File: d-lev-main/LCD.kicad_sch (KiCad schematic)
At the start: 9 parts, among them Q1 MMBT3904

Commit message: clean up 3d models
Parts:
- DS2: footprint LCD_LCD-20X4B -> d-lev:ERM2004-1
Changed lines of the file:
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@@
       (effects (font (size 1.27 1.27)))
     )
-    (property "Footprint" "LCD_LCD-20X4B" (at 149.86 102.87 0)
+    (property "Footprint" "d-lev:ERM2004-1" (at 149.86 102.87 0)
       (effects (font (size 1.27 1.27)) (justify bottom) hide)
     )

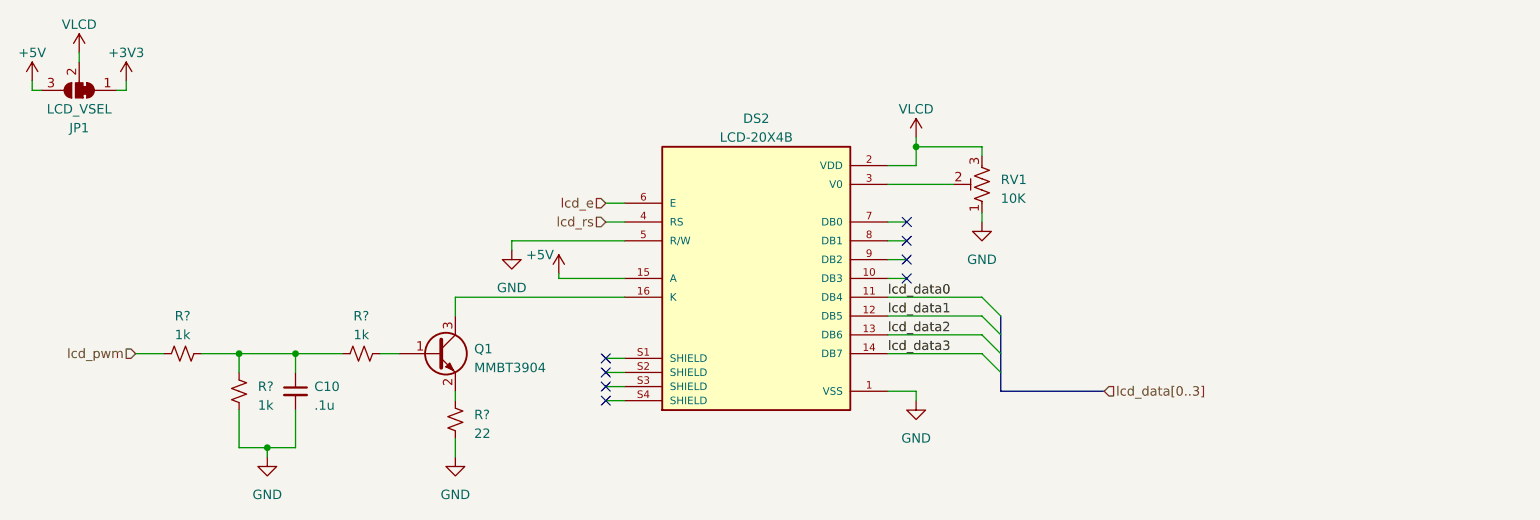
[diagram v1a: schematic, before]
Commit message: Level shifters and rearrange encoders
* WIP: use net buses more effectively to organize encoder signals
* Add application note for level shifters
* Add level shifters for UART, change MIDI level shifter BJT to FET
* Add MIDI_HI pull-up on d-lev-io board
* Add/change some footprints
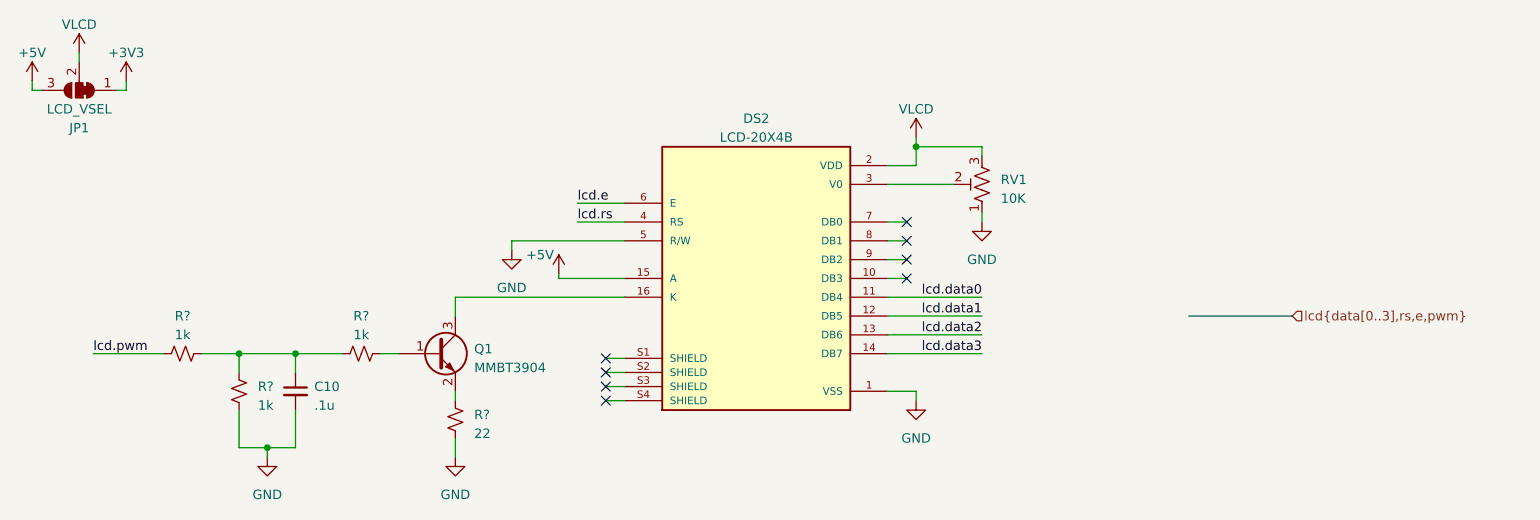
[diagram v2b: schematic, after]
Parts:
- C10: footprint (none) -> Capacitor_SMD:C_0805_2012Metric_Pad1.18x1.45mm_HandSolder
- JP1: footprint (none) -> Jumper:SolderJumper-3_P1.3mm_Bridged2Bar12_RoundedPad1.0x1.5mm_NumberLabels
- R? (x4): footprint (none) -> Resistor_SMD:R_0805_2012Metric_Pad1.20x1.40mm_HandSolder
- RV1: footprint (none) -> Potentiometer_SMD:Potentiometer_Bourns_3269P_Horizontal
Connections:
- net lcd_data0 renamed lcd.data0
- net lcd_data1 renamed lcd.data1
- net lcd_data2 renamed lcd.data2
- net lcd_data3 renamed lcd.data3
- net lcd_e renamed lcd.e
- net lcd_pwm renamed lcd.pwm
- net lcd_rs renamed lcd.rs
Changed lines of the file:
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@@
   (no_connect (at 129.54 115.57))
   (no_connect (at 170.18 102.87))
-  (bus_entry (at 180.34 105.41) (size 2.54 2.54)
-    (stroke (width 0) (type default))
-  )
-  (bus_entry (at 180.34 107.95) (size 2.54 2.54)
-    (stroke (width 0) (type default))
-  )
-  (bus_entry (at 180.34 110.49) (size 2.54 2.54)
-    (stroke (width 0) (type default))
-  )
-  (bus_entry (at 180.34 113.03) (size 2.54 2.54)
-    (stroke (width 0) (type default))
-  )
   (wire (pts (xy 80.01 125.73) (xy 83.82 125.73))
     (stroke (width 0) (type default))
@@
     (stroke (width 0) (type default))
   )
-  (wire (pts (xy 129.54 95.25) (xy 132.08 95.25))
+  (wire (pts (xy 125.73 95.25) (xy 132.08 95.25))
     (stroke (width 0) (type default))
   )
@@
     (stroke (width 0) (type default))
   )
-  (bus (pts (xy 182.88 107.95) (xy 182.88 110.49))
-    (stroke (width 0) (type default))
-  )
   (wire (pts (xy 132.08 115.57) (xy 129.54 115.57))
     (stroke (width 0) (type default))
@@
     (stroke (width 0) (type default))
   )
+  (wire (pts (xy 60.325 113.03) (xy 69.85 113.03))
+    (stroke (width 0) (type default))
+  )
   (wire (pts (xy 99.06 113.03) (xy 101.6 113.03))
     (stroke (width 0) (type default))
@@
     (stroke (width 0) (type default))
   )
-  (bus (pts (xy 196.85 118.11) (xy 182.88 118.11))
+  (bus (pts (xy 222.25 107.95) (xy 208.28 107.95))
     (stroke (width 0) (type default))
   )
@@
     (stroke (width 0) (type default))
   )
-  (wire (pts (xy 66.04 113.03) (xy 69.85 113.03))
-    (stroke (width 0) (type default))
-  )
-  (bus (pts (xy 182.88 110.49) (xy 182.88 113.03))
-    (stroke (width 0) (type default))
-  )
-  (wire (pts (xy 129.54 92.71) (xy 132.08 92.71))
+  (wire (pts (xy 125.73 92.71) (xy 132.08 92.71))
     (stroke (width 0) (type default))
   )
@@
     (stroke (width 0) (type default))
   )
-  (bus (pts (xy 182.88 113.03) (xy 182.88 115.57))
-    (stroke (width 0) (type default))
-  )
   (wire (pts (xy 171.45 85.09) (xy 171.45 87.63))
     (stroke (width 0) (type default))
@@
     (stroke (width 0) (type default))
   )
-  (bus (pts (xy 182.88 118.11) (xy 182.88 115.57))
-    (stroke (width 0) (type default))
-  )
   (wire (pts (xy 171.45 83.82) (xy 171.45 85.09))
     (stroke (width 0) (type default))
@@
     (stroke (width 0) (type default))
   )
-  (label "lcd_data0" (at 167.64 105.41 0) (fields_autoplaced)
+  (label "lcd.data2" (at 180.34 110.49 180) (fields_autoplaced)
+    (effects (font (size 1.27 1.27)) (justify right bottom))
+  )
+  (label "lcd.rs" (at 125.73 95.25 0) (fields_autoplaced)
     (effects (font (size 1.27 1.27)) (justify left bottom))
   )
-  (label "lcd_data3" (at 167.64 113.03 0) (fields_autoplaced)
+  (label "lcd.e" (at 125.73 92.71 0) (fields_autoplaced)
     (effects (font (size 1.27 1.27)) (justify left bottom))
   )
-  (label "lcd_data2" (at 167.64 110.49 0) (fields_autoplaced)
+  (label "lcd.pwm" (at 60.325 113.03 0) (fields_autoplaced)
     (effects (font (size 1.27 1.27)) (justify left bottom))
   )
-  (label "lcd_data1" (at 167.64 107.95 0) (fields_autoplaced)
-    (effects (font (size 1.27 1.27)) (justify left bottom))
-  )
-  (hierarchical_label "lcd_data[0..3]" (shape input) (at 196.85 118.11 0) (fields_autoplaced)
+  (label "lcd.data0" (at 180.34 105.41 180) (fields_autoplaced)
+    (effects (font (size 1.27 1.27)) (justify right bottom))
+  )
+  (label "lcd.data1" (at 180.34 107.95 180) (fields_autoplaced)
+    (effects (font (size 1.27 1.27)) (justify right bottom))
+  )
+  (label "lcd.data3" (at 180.34 113.03 180) (fields_autoplaced)
+    (effects (font (size 1.27 1.27)) (justify right bottom))
+  )
+  (hierarchical_label "lcd{data[0..3],rs,e,pwm}" (shape input) (at 222.25 107.95 0) (fields_autoplaced)
     (effects (font (size 1.27 1.27)) (justify left))
-  )
-  (hierarchical_label "lcd_pwm" (shape input) (at 66.04 113.03 180) (fields_autoplaced)
-    (effects (font (size 1.27 1.27)) (justify right))
-  )
-  (hierarchical_label "lcd_rs" (shape input) (at 129.54 95.25 180) (fields_autoplaced)
-    (effects (font (size 1.27 1.27)) (justify right))
-  )
-  (hierarchical_label "lcd_e" (shape input) (at 129.54 92.71 180) (fields_autoplaced)
-    (effects (font (size 1.27 1.27)) (justify right))
   )
   (symbol (lib_id "power:+3V3") (at 64.77 76.2 0) (unit 1)
@@
       (effects (font (size 1.27 1.27)))
     )
-    (property "Footprint" "" (at 72.39 113.03 0)
+    (property "Footprint" "Resistor_SMD:R_0805_2012Metric_Pad1.20x1.40mm_HandSolder" (at 72.39 113.03 0)
       (effects (font (size 1.27 1.27)) hide)
     )
@@
       (effects (font (size 1.27 1.27)))
     )
-    (property "Footprint" "" (at 96.52 113.03 0)
+    (property "Footprint" "Resistor_SMD:R_0805_2012Metric_Pad1.20x1.40mm_HandSolder" (at 96.52 113.03 0)
       (effects (font (size 1.27 1.27)) hide)
     )
@@
       (effects (font (size 1.27 1.27)) (justify right))
     )
-    (property "Footprint" "" (at 109.22 121.92 0)
+    (property "Footprint" "Resistor_SMD:R_0805_2012Metric_Pad1.20x1.40mm_HandSolder" (at 109.22 121.92 0)
       (effects (font (size 1.27 1.27)) hide)
     )
@@
       (effects (font (size 1.27 1.27)) (justify left))
     )
-    (property "Footprint" "" (at 87.63 118.11 0)
+    (property "Footprint" "Capacitor_SMD:C_0805_2012Metric_Pad1.18x1.45mm_HandSolder" (at 87.63 118.11 0)
       (effects (font (size 1.27 1.27)) hide)
     )
@@
       (effects (font (size 1.27 1.27)) (justify right))
     )
-    (property "Footprint" "" (at 180.34 90.17 0)
+    (property "Footprint" "Potentiometer_SMD:Potentiometer_Bourns_3269P_Horizontal" (at 180.34 90.17 0)
       (effects (font (size 1.27 1.27)) hide)
     )
@@
       (effects (font (size 1.27 1.27)))
     )
-    (property "Footprint" "" (at 58.42 77.47 0)
+    (property "Footprint" "Jumper:SolderJumper-3_P1.3mm_Bridged2Bar12_RoundedPad1.0x1.5mm_NumberLabels" (at 58.42 77.47 0)
       (effects (font (size 1.27 1.27)) hide)
     )
@@
       (effects (font (size 1.27 1.27)) (justify right))
     )
-    (property "Footprint" "" (at 80.01 118.11 0)
-      (effects (font (size 1.27 1.27)) hide)
-    )
+    (property "Footprint" "Resistor_SMD:R_0805_2012Metric_Pad1.20x1.40mm_HandSolder" (at 80.01 118.11 0)
+      (effects (font (size 1.27 1.27)) hide)
+    )

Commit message: Small changes to 3D models and footprints; fixed bus routing of encoder signals
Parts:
- DS2: footprint d-lev:ERM2004-1 -> d-lev:ERM2004-0
- RV1: footprint Potentiometer_SMD:Potentiometer_Bourns_3269P_Horizontal -> Potentiometer_SMD:Potentiometer_Bourns_TC33X_Vertical
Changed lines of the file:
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@@
       (effects (font (size 1.27 1.27)))
     )
-    (property "Footprint" "d-lev:ERM2004-1" (at 149.86 102.87 0)
+    (property "Footprint" "d-lev:ERM2004-0" (at 149.86 102.87 0)
       (effects (font (size 1.27 1.27)) (justify bottom) hide)
     )
@@
       (effects (font (size 1.27 1.27)) (justify right))
     )
-    (property "Footprint" "Potentiometer_SMD:Potentiometer_Bourns_3269P_Horizontal" (at 180.34 90.17 0)
-      (effects (font (size 1.27 1.27)) hide)
-    )
+    (property "Footprint" "Potentiometer_SMD:Potentiometer_Bourns_TC33X_Vertical" (at 180.34 90.17 0)
+      (effects (font (size 1.27 1.27)) hide)
+    )

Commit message: start routing
* add simple knob model
* place encoders
* change display to use SMT female headers and SMTSO screw holes
* rotate fpga model 90 degrees
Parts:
- added H5, H6, H7, H8: M3 Standoff, d-lev:SMTSO-M3, symbol Mechanical:MountingHole_Pad
- DS2: value LCD-20X4B -> LCD-20X4B-noshield; footprint d-lev:ERM2004-0 -> d-lev:ERM2004-2; symbol assorted:LCD-20X4B -> assorted:LCD-20X4B-noshield
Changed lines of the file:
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@@
   (junction (at 83.82 125.73) (diameter 0) (color 0 0 0 0)
   )
-  (no_connect (at 129.54 117.475))
-  (no_connect (at 129.54 119.38))
+  (no_connect (at 193.04 93.98))
+  (no_connect (at 193.04 88.9))
   (no_connect (at 170.18 100.33))
   (no_connect (at 170.18 97.79))
   (no_connect (at 170.18 95.25))
-  (no_connect (at 129.54 113.665))
-  (no_connect (at 129.54 115.57))
+  (no_connect (at 193.04 99.06))
   (no_connect (at 170.18 102.87))
+  (no_connect (at 193.04 83.82))
   (wire (pts (xy 80.01 125.73) (xy 83.82 125.73))
     (stroke (width 0) (type default))
   )
+  (wire (pts (xy 195.58 99.06) (xy 193.04 99.06))
+    (stroke (width 0) (type default))
+  )
   (wire (pts (xy 167.64 95.25) (xy 170.18 95.25))
     (stroke (width 0) (type default))
@@
     (stroke (width 0) (type default))
   )
+  (wire (pts (xy 195.58 88.9) (xy 193.04 88.9))
+    (stroke (width 0) (type default))
+  )
   (wire (pts (xy 52.07 77.47) (xy 53.34 77.47))
     (stroke (width 0) (type default))
@@
     (stroke (width 0) (type default))
   )
-  (wire (pts (xy 132.08 115.57) (xy 129.54 115.57))
-    (stroke (width 0) (type default))
-  )
   (wire (pts (xy 167.64 118.11) (xy 171.45 118.11))
     (stroke (width 0) (type default))
@@
     (stroke (width 0) (type default))
   )
-  (wire (pts (xy 132.08 113.665) (xy 129.54 113.665))
-    (stroke (width 0) (type default))
-  )
   (wire (pts (xy 87.63 115.57) (xy 87.63 113.03))
     (stroke (width 0) (type default))
@@
     (stroke (width 0) (type default))
   )
+  (wire (pts (xy 195.58 83.82) (xy 193.04 83.82))
+    (stroke (width 0) (type default))
+  )
   (wire (pts (xy 83.82 125.73) (xy 87.63 125.73))
     (stroke (width 0) (type default))
   )
-  (wire (pts (xy 132.08 117.475) (xy 129.54 117.475))
-    (stroke (width 0) (type default))
-  )
   (wire (pts (xy 123.19 102.235) (xy 123.19 102.87))
     (stroke (width 0) (type default))
@@
     (stroke (width 0) (type default))
   )
-  (wire (pts (xy 132.08 119.38) (xy 129.54 119.38))
-    (stroke (width 0) (type default))
-  )
   (wire (pts (xy 109.22 118.11) (xy 109.22 119.38))
     (stroke (width 0) (type default))
@@
   )
   (wire (pts (xy 167.64 100.33) (xy 170.18 100.33))
+    (stroke (width 0) (type default))
+  )
+  (wire (pts (xy 195.58 93.98) (xy 193.04 93.98))
     (stroke (width 0) (type default))
   )
@@
     )
   )
+  (symbol (lib_id "Mechanical:MountingHole_Pad") (at 198.12 99.06 270) (unit 1)
+    (in_bom yes) (on_board yes) (dnp no) (fields_autoplaced)
+    (property "Reference" "H8" (at 201.93 98.425 90)
+      (effects (font (size 1.27 1.27)) (justify left))
+    )
+    (property "Value" "M3 Standoff" (at 201.93 100.965 90)
+      (effects (font (size 1.27 1.27)) (justify left))
+    )
+    (property "Footprint" "d-lev:SMTSO-M3" (at 198.12 99.06 0)
+      (effects (font (size 1.27 1.27)) hide)
+    )
+    (property "Datasheet" "~" (at 198.12 99.06 0)
+      (effects (font (size 1.27 1.27)) hide)
+    )
+    (pin "1")
+    (instances
+      (project "dlev-mini"
+        (path "/eb5e8bfd-9871-4528-bf57-58851bf63907/2925ec6e-2aba-4938-a246-f8cb5ac94723"
+          (reference "H8") (unit 1)
+        )
+      )
+    )
+  )
   (symbol (lib_id "Device:R_Small_US") (at 72.39 113.03 90) (unit 1)
     (in_bom yes) (on_board yes) (dnp no) (fields_autoplaced)
@@
         (path "/eb5e8bfd-9871-4528-bf57-58851bf63907/2925ec6e-2aba-4938-a246-f8cb5ac94723"
           (reference "R5") (unit 1)
+        )
+      )
+    )
+  )
+  (symbol (lib_id "Mechanical:MountingHole_Pad") (at 198.12 93.98 270) (unit 1)
+    (in_bom yes) (on_board yes) (dnp no) (fields_autoplaced)
+    (property "Reference" "H7" (at 201.93 93.345 90)
+      (effects (font (size 1.27 1.27)) (justify left))
+    )
+    (property "Value" "M3 Standoff" (at 201.93 95.885 90)
+      (effects (font (size 1.27 1.27)) (justify left))
+    )
+    (property "Footprint" "d-lev:SMTSO-M3" (at 198.12 93.98 0)
+      (effects (font (size 1.27 1.27)) hide)
+    )
+    (property "Datasheet" "~" (at 198.12 93.98 0)
+      (effects (font (size 1.27 1.27)) hide)
+    )
+    (pin "1")
+    (instances
+      (project "dlev-mini"
+        (path "/eb5e8bfd-9871-4528-bf57-58851bf63907/2925ec6e-2aba-4938-a246-f8cb5ac94723"
+          (reference "H7") (unit 1)
         )
       )
@@
     )
   )
-  (symbol (lib_id "assorted:LCD-20X4B") (at 149.86 102.87 0) (unit 1)
+  (symbol (lib_id "assorted:LCD-20X4B-noshield") (at 149.86 102.87 0) (unit 1)
     (in_bom yes) (on_board yes) (dnp no) (fields_autoplaced)
     (property "Reference" "DS2" (at 149.86 81.28 0)
       (effects (font (size 1.27 1.27)))
     )
-    (property "Value" "LCD-20X4B" (at 149.86 83.82 0)
-      (effects (font (size 1.27 1.27)))
-    )
-    (property "Footprint" "d-lev:ERM2004-0" (at 149.86 102.87 0)
+    (property "Value" "LCD-20X4B-noshield" (at 149.86 83.82 0)
+      (effects (font (size 1.27 1.27)))
+    )
+    (property "Footprint" "d-lev:ERM2004-2" (at 149.86 102.87 0)
       (effects (font (size 1.27 1.27)) (justify bottom) hide)
     )
@@
     (pin "8")
     (pin "9")
-    (pin "S1")
-    (pin "S2")
-    (pin "S3")
-    (pin "S4")
     (instances
       (project "dlev-mini"
@@
         (path "/eb5e8bfd-9871-4528-bf57-58851bf63907/2925ec6e-2aba-4938-a246-f8cb5ac94723"
           (reference "#PWR043") (unit 1)
+        )
+      )
+    )
+  )
+  (symbol (lib_id "Mechanical:MountingHole_Pad") (at 198.12 83.82 270) (unit 1)
+    (in_bom yes) (on_board yes) (dnp no) (fields_autoplaced)
+    (property "Reference" "H5" (at 201.93 83.185 90)
+      (effects (font (size 1.27 1.27)) (justify left))
+    )
+    (property "Value" "M3 Standoff" (at 201.93 85.725 90)
+      (effects (font (size 1.27 1.27)) (justify left))
+    )
+    (property "Footprint" "d-lev:SMTSO-M3" (at 198.12 83.82 0)
+      (effects (font (size 1.27 1.27)) hide)
+    )
+    (property "Datasheet" "~" (at 198.12 83.82 0)
+      (effects (font (size 1.27 1.27)) hide)
+    )
+    (pin "1")
+    (instances
+      (project "dlev-mini"
+        (path "/eb5e8bfd-9871-4528-bf57-58851bf63907/2925ec6e-2aba-4938-a246-f8cb5ac94723"
+          (reference "H5") (unit 1)
         )
       )
@@
         )
       )
+    )
+  )
+  (symbol (lib_id "Mechanical:MountingHole_Pad") (at 198.12 88.9 270) (unit 1)
+    (in_bom yes) (on_board yes) (dnp no) (fields_autoplaced)
+    (property "Reference" "H6" (at 201.93 88.265 90)
+      (effects (font (size 1.27 1.27)) (justify left))
+    )
+    (property "Value" "M3 Standoff" (at 201.93 90.805 90)
+      (effects (font (size 1.27 1.27)) (justify left))
+    )
+    (property "Footprint" "d-lev:SMTSO-M3" (at 198.12 88.9 0)
+      (effects (font (size 1.27 1.27)) hide)
+    )
+    (property "Datasheet" "~" (at 198.12 88.9 0)
+      (effects (font (size 1.27 1.27)) hide)
+    )
+    (pin "1")
+    (instances
+      (project "dlev-mini"
+        (path "/eb5e8bfd-9871-4528-bf57-58851bf63907/2925ec6e-2aba-4938-a246-f8cb5ac94723"
+          (reference "H6") (unit 1)
+        )
+      )

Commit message: many changes to pcb
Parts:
- renumbered C10 to C21
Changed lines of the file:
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@@
   (symbol (lib_id "Device:C_Small") (at 87.63 118.11 0) (unit 1)
     (in_bom yes) (on_board yes) (dnp no) (fields_autoplaced)
-    (property "Reference" "C10" (at 90.17 117.4813 0)
+    (property "Reference" "C21" (at 90.17 117.4813 0)
       (effects (font (size 1.27 1.27)) (justify left))
     )
@@
       (project "dlev-mini"
         (path "/eb5e8bfd-9871-4528-bf57-58851bf63907/2925ec6e-2aba-4938-a246-f8cb5ac94723"
-          (reference "C10") (unit 1)
+          (reference "C21") (unit 1)
         )
       )

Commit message: Switch from Rpacks to 0603 pull resistors
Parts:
- removed Q1: MMBT3904, Package_TO_SOT_SMD:SOT-23, symbol Transistor_BJT:MMBT3904
- added Q4: BSS138, Package_TO_SOT_SMD:SOT-23, symbol Transistor_FET:BSS138
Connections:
- net at R?.2: now also Q4.1 (G)
- net at R?.2: now also Q4.3 (D)
- net at DS2.16 (K): now also Q4.2 (S)
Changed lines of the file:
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@@
-    )
-  )
-  (symbol (lib_id "Transistor_BJT:MMBT3904") (at 106.68 113.03 0) (unit 1)
-    (in_bom yes) (on_board yes) (dnp no) (fields_autoplaced)
-    (property "Reference" "Q1" (at 111.76 112.395 0)
-      (effects (font (size 1.27 1.27)) (justify left))
-    )
-    (property "Value" "MMBT3904" (at 111.76 114.935 0)
-      (effects (font (size 1.27 1.27)) (justify left))
-    )
-    (property "Footprint" "Package_TO_SOT_SMD:SOT-23" (at 111.76 114.935 0)
-      (effects (font (size 1.27 1.27) italic) (justify left) hide)
-    )
-    (property "Datasheet" "https://www.onsemi.com/pub/Collateral/2N3903-D.PDF" (at 106.68 113.03 0)
-      (effects (font (size 1.27 1.27)) (justify left) hide)
-    )
-    (pin "1")
-    (pin "2")
-    (pin "3")
-    (instances
-      (project "dlev-mini"
-        (path "/eb5e8bfd-9871-4528-bf57-58851bf63907"
-          (reference "Q1") (unit 1)
-        )
-        (path "/eb5e8bfd-9871-4528-bf57-58851bf63907/2925ec6e-2aba-4938-a246-f8cb5ac94723"
-          (reference "Q2") (unit 1)
-        )
-      )
     )
   )
@@
         )
       )
+    )
+  )
+  (symbol (lib_id "Transistor_FET:BSS138") (at 106.68 113.03 0) (mirror x) (unit 1)
+    (in_bom yes) (on_board yes) (dnp no)
+    (property "Reference" "Q4" (at 113.03 113.665 0)
+      (effects (font (size 1.27 1.27)) (justify left))
+    )
+    (property "Value" "BSS138" (at 113.03 111.125 0)
+      (effects (font (size 1.27 1.27)) (justify left))
+    )
+    (property "Footprint" "Package_TO_SOT_SMD:SOT-23" (at 111.76 111.125 0)
+      (effects (font (size 1.27 1.27) italic) (justify left) hide)
+    )
+    (property "Datasheet" "https://www.onsemi.com/pub/Collateral/BSS138-D.PDF" (at 106.68 113.03 0)
+      (effects (font (size 1.27 1.27)) (justify left) hide)
+    )
+    (pin "1")
+    (pin "2")
+    (pin "3")
+    (instances
+      (project "dlev-mini"
+        (path "/eb5e8bfd-9871-4528-bf57-58851bf63907"
+          (reference "Q4") (unit 1)
+        )
+        (path "/eb5e8bfd-9871-4528-bf57-58851bf63907/2925ec6e-2aba-4938-a246-f8cb5ac94723"
+          (reference "Q1") (unit 1)
+        )
+      )
